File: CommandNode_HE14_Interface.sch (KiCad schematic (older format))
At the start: 22 parts

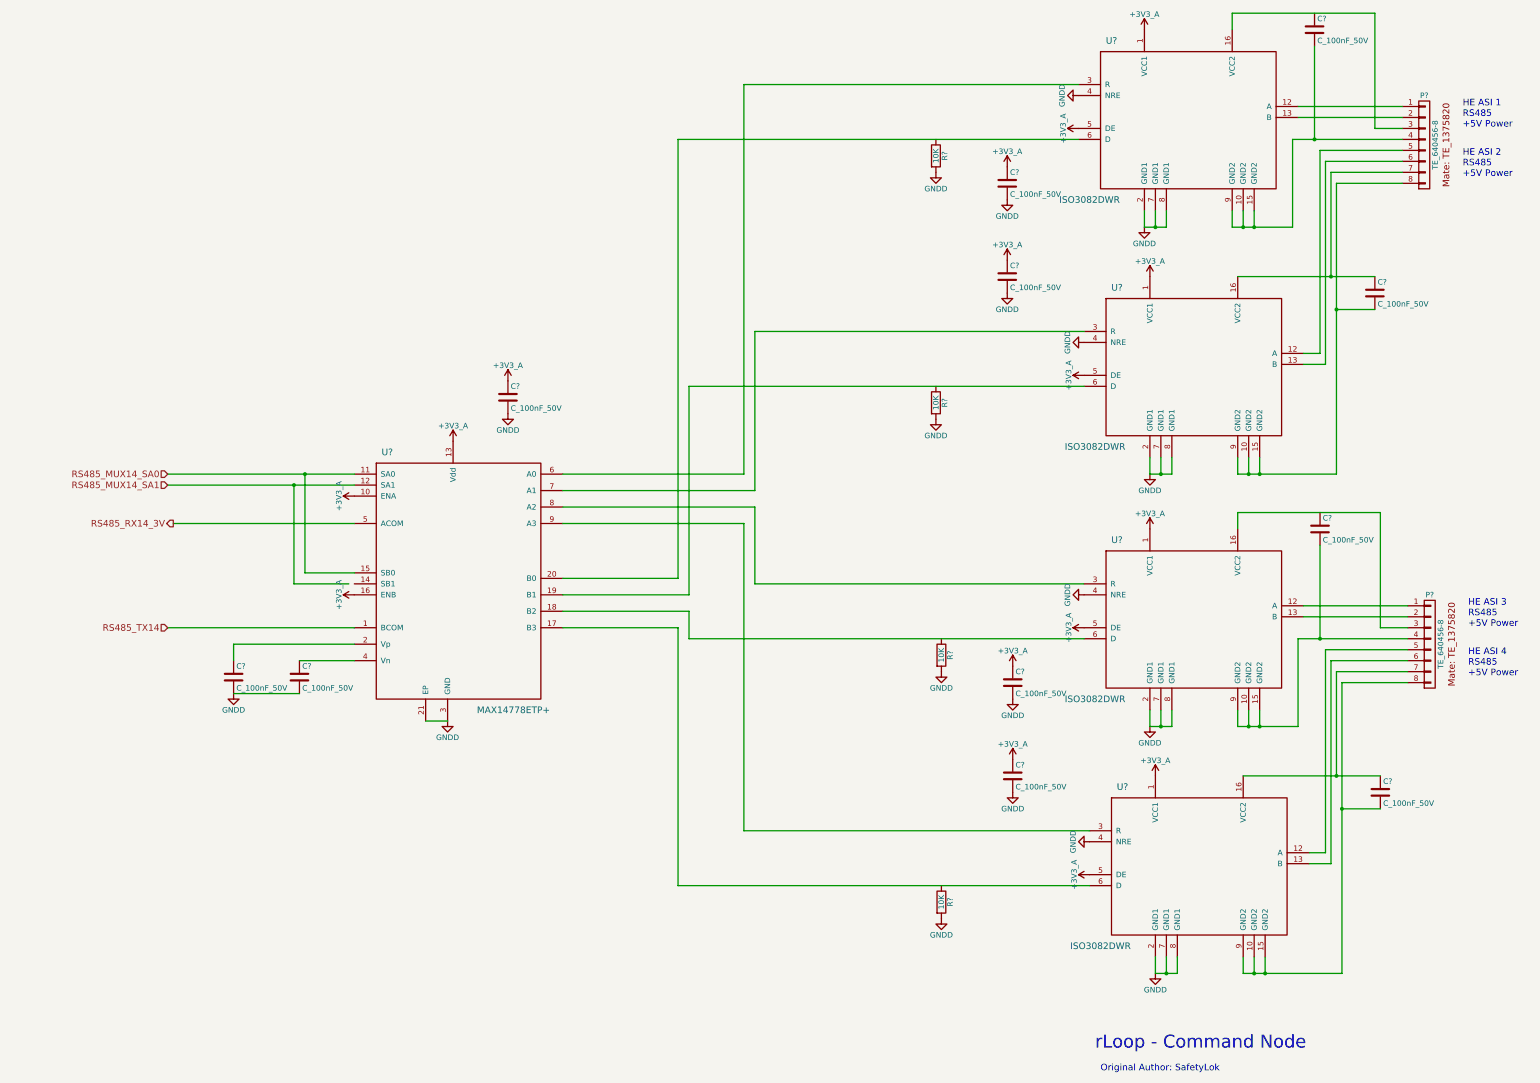
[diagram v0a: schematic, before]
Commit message: Finish and print schematics for review
Lifting mechanism, charger interface, Data Enable on HE controller
RS585, Park Brake and node core.
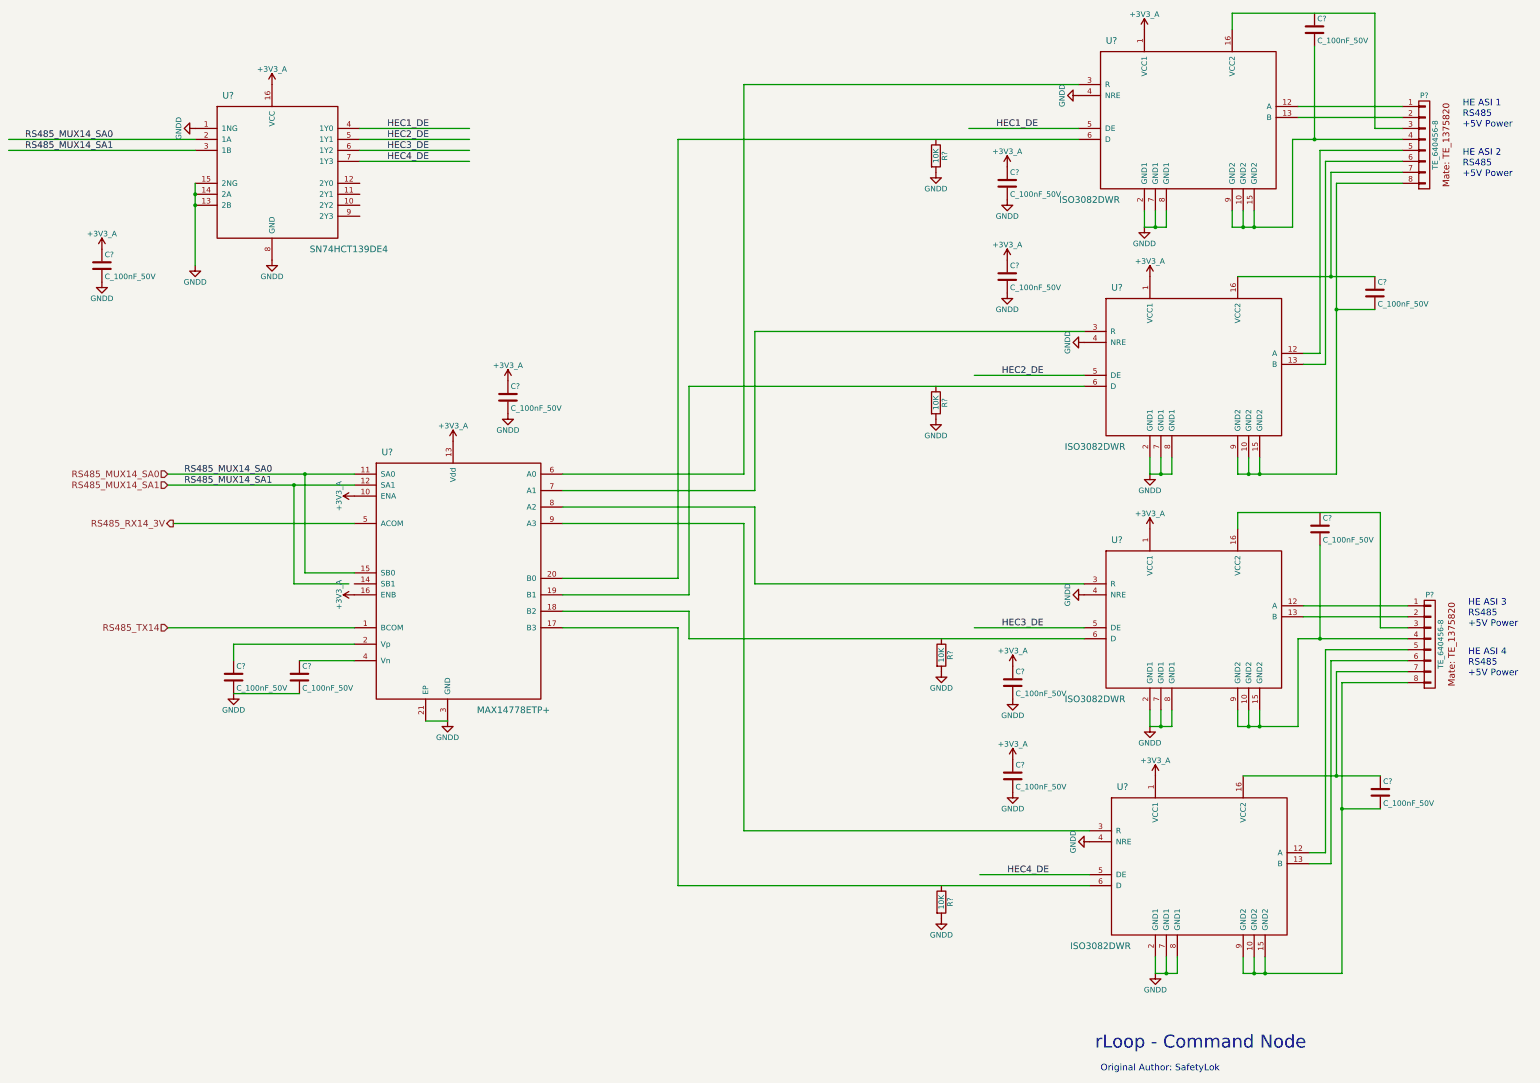
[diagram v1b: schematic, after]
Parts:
- added C?: C_100nF_50V, RLOOP_FOOTPRINTS:rLoop_C_0603, symbol C_100nF_50V
- added U?: SN74HCT139DE4, RLOOP_FOOTPRINTS:rLoop_SOIC_16, symbol SN74HCT139DE4
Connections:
- net labels added: HEC1_DE, HEC2_DE, HEC3_DE, HEC4_DE
- wire segments 111 -> 122
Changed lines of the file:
@@
 $Descr A3 16535 11693
 encoding utf-8
-Sheet 3 7
+Sheet 3 8
 Title "Hover Engine Interface"
 Date ""
@@
 	0    1    1    0
 $EndComp
-$Comp
-L +3V3_A #PWR?
-U 1 1 575D1E8C
-P 11750 1800
-F 0 "#PWR?" H 11750 1650 50  0001 C CNN
-F 1 "+3V3_A" H 11750 1940 50  0000 C CNN
-F 2 "" H 11750 1800 60  0000 C CNN
-F 3 "" H 11750 1800 60  0000 C CNN
-	1    11750 1800
-	0    -1   -1   0
-$EndComp
-$Comp
-L +3V3_A #PWR?
-U 1 1 575D1F27
-P 11800 4050
-F 0 "#PWR?" H 11800 3900 50  0001 C CNN
-F 1 "+3V3_A" H 11800 4190 50  0000 C CNN
-F 2 "" H 11800 4050 60  0000 C CNN
-F 3 "" H 11800 4050 60  0000 C CNN
-	1    11800 4050
-	0    -1   -1   0
-$EndComp
 Wire Wire Line
 	8200 4150 11800 4150
@@
 	0    1    1    0
 $EndComp
-$Comp
-L +3V3_A #PWR?
-U 1 1 575D2705
-P 11800 6350
-F 0 "#PWR?" H 11800 6200 50  0001 C CNN
-F 1 "+3V3_A" H 11800 6490 50  0000 C CNN
-F 2 "" H 11800 6350 60  0000 C CNN
-F 3 "" H 11800 6350 60  0000 C CNN
-	1    11800 6350
-	0    -1   -1   0
-$EndComp
-$Comp
-L +3V3_A #PWR?
-U 1 1 575D270B
-P 11850 8600
-F 0 "#PWR?" H 11850 8450 50  0001 C CNN
-F 1 "+3V3_A" H 11850 8740 50  0000 C CNN
-F 2 "" H 11850 8600 60  0000 C CNN
-F 3 "" H 11850 8600 60  0000 C CNN
-	1    11850 8600
-	0    -1   -1   0
-$EndComp
 Wire Wire Line
 	8100 8700 11850 8700
@@
 	4600 5950 4600 5050
 Connection ~ 4600 5050
+$Comp
+L SN74HCT139DE4 U?
+U 1 1 5769BEA2
+P 3900 1600
+F 0 "U?" H 4000 1700 60  0000 C CNN
+F 1 "SN74HCT139DE4" H 5100 300 60  0000 C CNN
+F 2 "RLOOP_FOOTPRINTS:rLoop_SOIC_16" H 3800 1500 60  0001 C CNN
+F 3 "" H 3900 1600 60  0000 C CNN
+	1    3900 1600
+	1    0    0    -1
+$EndComp
+$Comp
+L C_100nF_50V C?
+U 1 1 5769BF47
+P 2850 3050
+F 0 "C?" H 2875 3150 50  0000 L CNN
+F 1 "C_100nF_50V" H 2875 2950 50  0000 L CNN
+F 2 "RLOOP_FOOTPRINTS:rLoop_C_0603" H 2888 2900 50  0001 C CNN
+F 3 "" H 2850 3050 50  0000 C CNN
+	1    2850 3050
+	1    0    0    -1
+$EndComp
+$Comp
+L GNDD #PWR?
+U 1 1 5769BF4D
+P 2850 3200
+F 0 "#PWR?" H 2850 2950 50  0001 C CNN
+F 1 "GNDD" H 2850 3050 50  0000 C CNN
+F 2 "" H 2850 3200 50  0000 C CNN
+F 3 "" H 2850 3200 50  0000 C CNN
+	1    2850 3200
+	1    0    0    -1
+$EndComp
+$Comp
+L +3V3_A #PWR?
+U 1 1 5769BF53
+P 2850 2900
+F 0 "#PWR?" H 2850 2750 50  0001 C CNN
+F 1 "+3V3_A" H 2850 3040 50  0000 C CNN
+F 2 "" H 2850 2900 60  0000 C CNN
+F 3 "" H 2850 2900 60  0000 C CNN
+	1    2850 2900
+	1    0    0    -1
+$EndComp
+$Comp
+L GNDD #PWR?
+U 1 1 5769BF71
+P 4400 3000
+F 0 "#PWR?" H 4400 2750 50  0001 C CNN
+F 1 "GNDD" H 4400 2850 50  0000 C CNN
+F 2 "" H 4400 3000 50  0000 C CNN
+F 3 "" H 4400 3000 50  0000 C CNN
+	1    4400 3000
+	1    0    0    -1
+$EndComp
+$Comp
+L +3V3_A #PWR?
+U 1 1 5769BF91
+P 4400 1400
+F 0 "#PWR?" H 4400 1250 50  0001 C CNN
+F 1 "+3V3_A" H 4400 1540 50  0000 C CNN
+F 2 "" H 4400 1400 60  0000 C CNN
+F 3 "" H 4400 1400 60  0000 C CNN
+	1    4400 1400
+	1    0    0    -1
+$EndComp
+$Comp
+L GNDD #PWR?
+U 1 1 5769C071
+P 3700 3050
+F 0 "#PWR?" H 3700 2800 50  0001 C CNN
+F 1 "GNDD" H 3700 2900 50  0000 C CNN
+F 2 "" H 3700 3050 50  0000 C CNN
+F 3 "" H 3700 3050 50  0000 C CNN
+	1    3700 3050
+	1    0    0    -1
+$EndComp
+Wire Wire Line
+	3700 2300 3700 3050
+Connection ~ 3700 2400
+Connection ~ 3700 2500
+Wire Wire Line
+	10750 1800 11750 1800
+Text Label 11000 1800 0    60   ~ 0
+HEC1_DE
+Wire Wire Line
+	5200 1900 6200 1900
+Text Label 5450 1900 0    60   ~ 0
+HEC2_DE
+Wire Wire Line
+	5200 2000 6200 2000
+Text Label 5450 2000 0    60   ~ 0
+HEC3_DE
+Wire Wire Line
+	5200 2100 6200 2100
+Text Label 5450 2100 0    60   ~ 0
+HEC4_DE
+Wire Wire Line
+	10800 4050 11800 4050
+Text Label 11050 4050 0    60   ~ 0
+HEC2_DE
+Wire Wire Line
+	10800 6350 11800 6350
+Text Label 11050 6350 0    60   ~ 0
+HEC3_DE
+Wire Wire Line
+	10850 8600 11850 8600
+Text Label 11100 8600 0    60   ~ 0
+HEC4_DE
+$Comp
+L GNDD #PWR?
+U 1 1 5769E4A3
+P 3700 1800
+F 0 "#PWR?" H 3700 1550 50  0001 C CNN
+F 1 "GNDD" H 3700 1650 50  0000 C CNN
+F 2 "" H 3700 1800 50  0000 C CNN
+F 3 "" H 3700 1800 50  0000 C CNN
+	1    3700 1800
+	0    1    1    0
+$EndComp
+Wire Wire Line
+	2000 1900 3700 1900
+Wire Wire Line
+	2000 2000 3700 2000
+Text Label 2150 1900 0    60   ~ 0
+RS485_MUX14_SA0
+Text Label 2150 2000 0    60   ~ 0
+RS485_MUX14_SA1
+Wire Wire Line
+	5200 1800 6200 1800
+Text Label 5450 1800 0    60   ~ 0
+HEC1_DE
+Text Label 3600 4950 0    60   ~ 0
+RS485_MUX14_SA0
+Text Label 3600 5050 0    60   ~ 0
+RS485_MUX14_SA1
 $EndSCHEMATC
